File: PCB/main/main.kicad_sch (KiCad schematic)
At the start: 4 parts, among them J1 Conn_01x33_Female, J2 Conn_01x33_Female, J3 Conn_01x33_Female, J4 Conn_01x33_Female

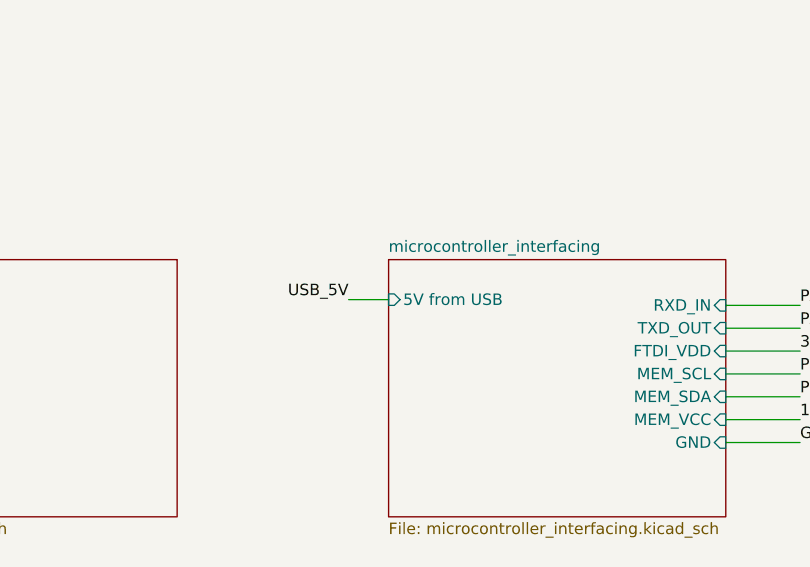
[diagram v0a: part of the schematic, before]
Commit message: Ran ERC and DRV
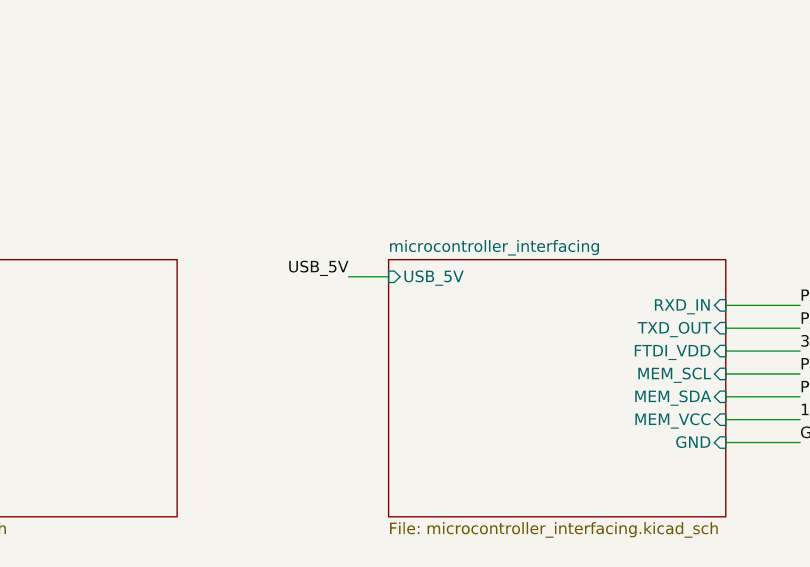
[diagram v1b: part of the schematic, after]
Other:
- sheet microcontroller_interfacing ports: added USB_5V; removed 5V from USB
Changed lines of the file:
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@@
-    (stroke (width 0) (type default) (color 0 0 0 0))
-  )
-  (wire (pts (xy 109.855 48.895) (xy 114.3 48.895))
     (stroke (width 0) (type default) (color 0 0 0 0))
   )
@@
   )
   (wire (pts (xy 45.72 97.79) (xy 53.34 97.79))
+    (stroke (width 0) (type default) (color 0 0 0 0))
+  )
+  (wire (pts (xy 109.855 46.355) (xy 114.3 46.355))
     (stroke (width 0) (type default) (color 0 0 0 0))
   )
@@
     (effects (font (size 1.27 1.27)) (justify left bottom))
   )
-  (label "USB_5V" (at 109.855 48.895 180)
+  (label "USB_5V" (at 109.855 46.355 180)
     (effects (font (size 1.27 1.27)) (justify right bottom))
   )
@@
       (effects (font (size 1.27 1.27)) (justify right))
     )
-    (pin "5V from USB" input (at 114.3 48.895 180)
-      (effects (font (size 1.27 1.27)) (justify left))
-    )
+    (pin "USB_5V" input (at 114.3 46.355 180)
+      (effects (font (size 1.27 1.27)) (justify left))
+    )

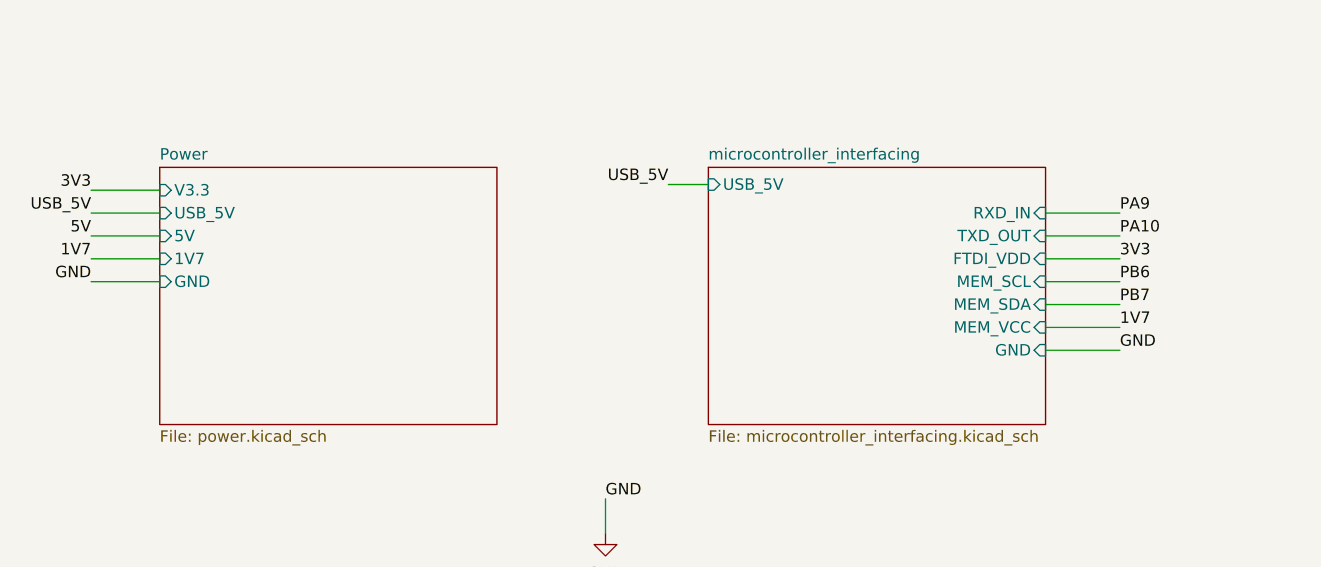
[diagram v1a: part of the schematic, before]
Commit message: Updated MC Interfacing with pullups
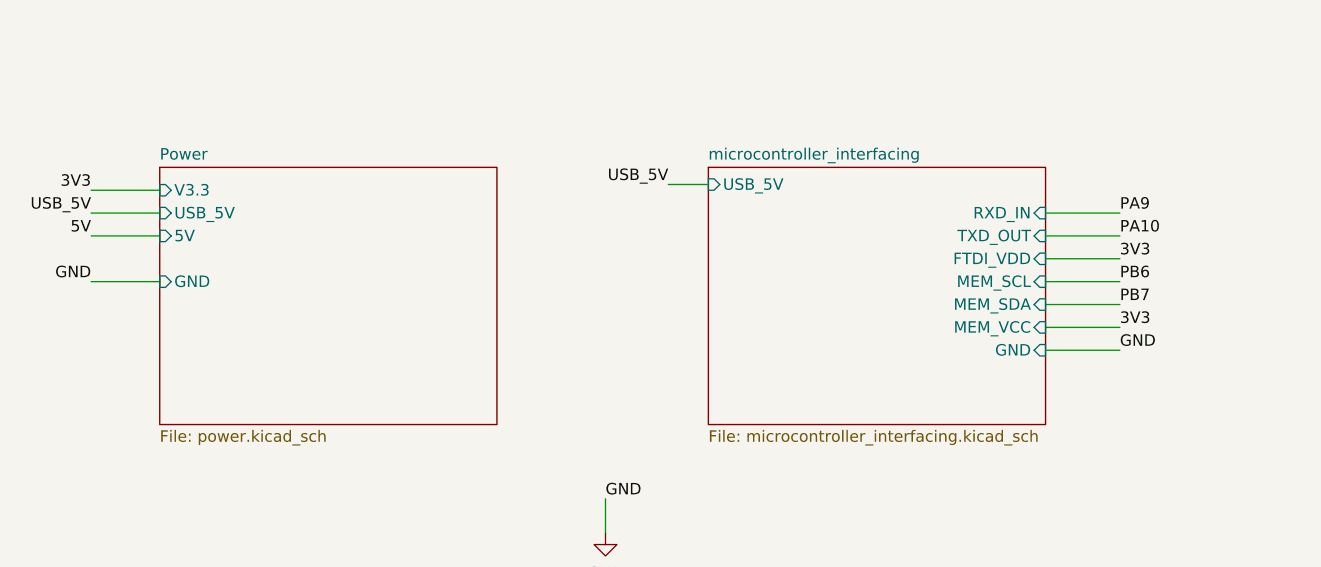
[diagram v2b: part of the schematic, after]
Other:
- sheet Power ports: added none; removed 1V7
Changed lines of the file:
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@@
-    (stroke (width 0) (type default) (color 0 0 0 0))
-  )
-  (wire (pts (xy 45.72 54.61) (xy 53.34 54.61))
     (stroke (width 0) (type default) (color 0 0 0 0))
   )
@@
     (effects (font (size 1.27 1.27)) (justify left bottom))
   )
-  (label "1V7" (at 160.02 62.23 0)
-    (effects (font (size 1.27 1.27)) (justify left bottom))
-  )
   (label "PC2" (at 211.455 54.61 0)
     (effects (font (size 1.27 1.27)) (justify left bottom))
@@
     (effects (font (size 1.27 1.27)) (justify left bottom))
   )
+  (label "3V3" (at 160.02 62.23 0)
+    (effects (font (size 1.27 1.27)) (justify left bottom))
+  )
   (label "PA8" (at 248.285 85.09 0)
     (effects (font (size 1.27 1.27)) (justify left bottom))
@@
   (label "NRST" (at 211.455 46.99 0)
     (effects (font (size 1.27 1.27)) (justify left bottom))
-  )
-  (label "1V7" (at 45.72 54.61 180)
-    (effects (font (size 1.27 1.27)) (justify right bottom))
   )
   (label "PC3" (at 229.235 57.15 0)
@@
       (effects (font (size 1.27 1.27)) (justify left))
     )
-    (pin "1V7" input (at 53.34 54.61 180)
-      (effects (font (size 1.27 1.27)) (justify left))
-    )
     (pin "GND" input (at 53.34 57.15 180)
       (effects (font (size 1.27 1.27)) (justify left))
@@
       (reference "R7") (unit 1) (value "1K2") (footprint "EEE3088F_Footprints:RESC1608X55N")
     )
-    (path "/d15c8919-7ccc-44b2-8fc4-b04c1b47b6fa/ddcc6717-e01a-4bd2-be17-1cca69bb6b0c"
-      (reference "R8") (unit 1) (value "1K8") (footprint "EEE3088F_Footprints:RESC1608X55N")
-    )
-    (path "/d15c8919-7ccc-44b2-8fc4-b04c1b47b6fa/e6d1bcb0-8f0e-405d-a7c1-88d99b710222"
-      (reference "R9") (unit 1) (value "1K8") (footprint "EEE3088F_Footprints:RESC1608X55N")
-    )
-    (path "/d15c8919-7ccc-44b2-8fc4-b04c1b47b6fa/5a5a09d7-5694-470c-a9d6-f9cfe31a44b2"
-      (reference "R10") (unit 1) (value "120R") (footprint "EEE3088F_Footprints:R0603")
-    )
     (path "/59b42903-2dc7-4011-ab5b-d7b81bd233c3/47c66d76-097b-43cf-8a5c-3288ec09b32f"
       (reference "R11") (unit 1) (value "1K2") (footprint "EEE3088F_Footprints:RESC1608X55N")
@@
       (reference "R13") (unit 1) (value "1K2") (footprint "EEE3088F_Footprints:RESC1608X55N")
     )
+    (path "/59b42903-2dc7-4011-ab5b-d7b81bd233c3/720239d4-cfc8-47b4-a18a-41a7b4226027"
+      (reference "R14") (unit 1) (value "10k") (footprint "EEE3088F_Footprints:R0603")
+    )
+    (path "/59b42903-2dc7-4011-ab5b-d7b81bd233c3/878c26d9-541e-4419-bfd9-495c7a099ac8"
+      (reference "R15") (unit 1) (value "10k") (footprint "EEE3088F_Footprints:R0603")
+    )
     (path "/cf6c12a4-3d95-473d-bafe-8be3892a84e9/7228bdfc-95f0-4c15-b9fb-cf288b667432"
